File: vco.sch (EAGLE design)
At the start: 23 parts, among them IC2 CEM3340

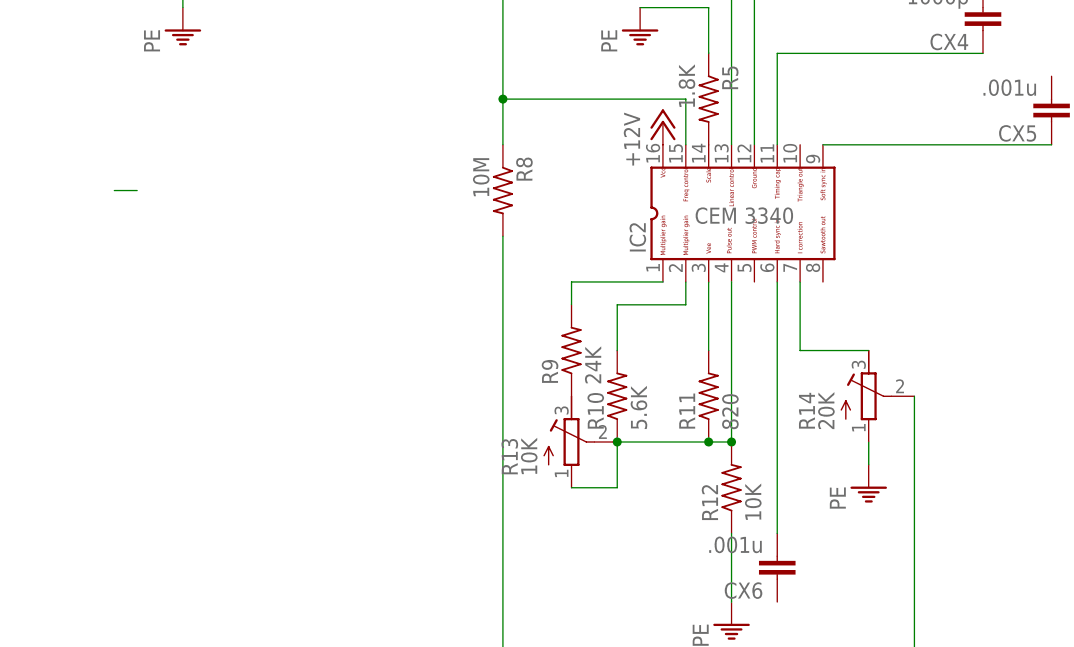
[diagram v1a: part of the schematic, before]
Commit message: Changed pots, added connector, updated org file.
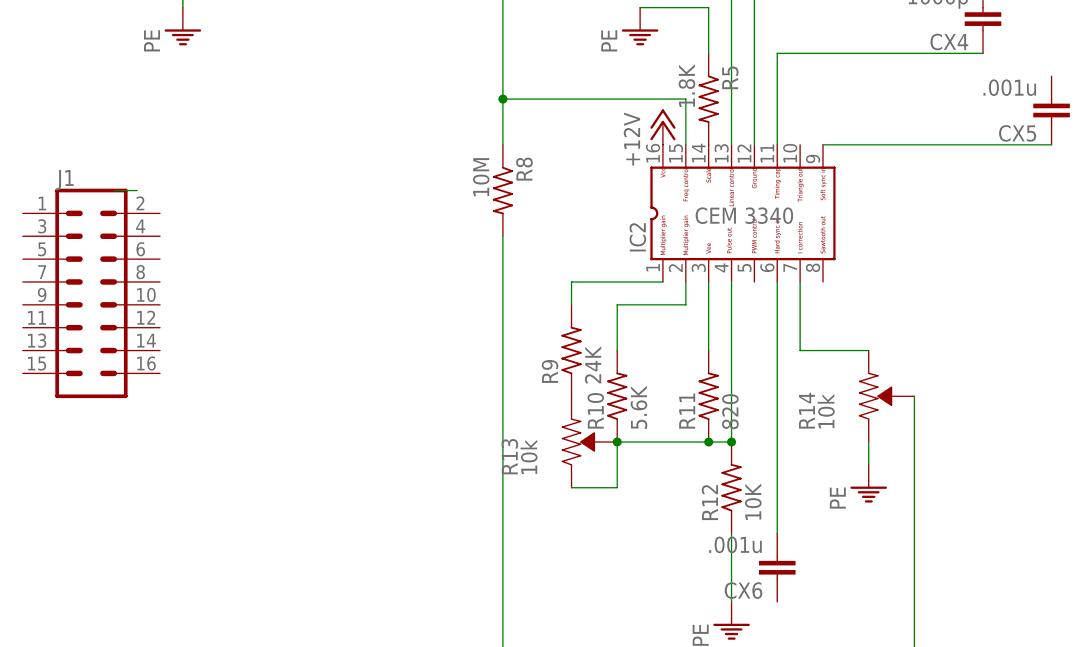
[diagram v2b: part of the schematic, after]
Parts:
- added J1: (no value), SparkFun-Connectors:CONN_08X2_SHROUD
- R13: value 10K -> 10k; device rcl:R-TRIMM4G/J -> SparkFun-Resistors:TRIMPOT-PTH-10MM-KNOB-1/2W-10%
- R14: value 20K -> 10k; device rcl:R-TRIMM4G/J -> SparkFun-Resistors:TRIMPOT-PTH-10MM-KNOB-1/2W-10%
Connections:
- net N$11: now also R13.CCW; no longer R13.E
- net N$13: now also R14.CCW; no longer R14.E
- net N$14: now also R13.CW, R13.WIPER; no longer R13.A, R13.S
- net N$17: now also R14.WIPER; no longer R14.S
- net PE: now also R14.CW; no longer R14.A

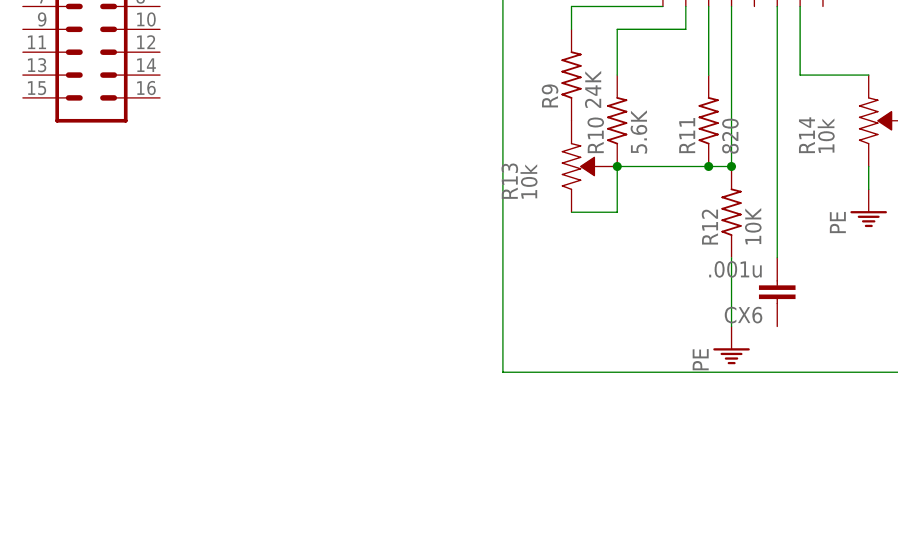
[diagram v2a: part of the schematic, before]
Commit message: Added -5v regulator as option. fixed pin 4.
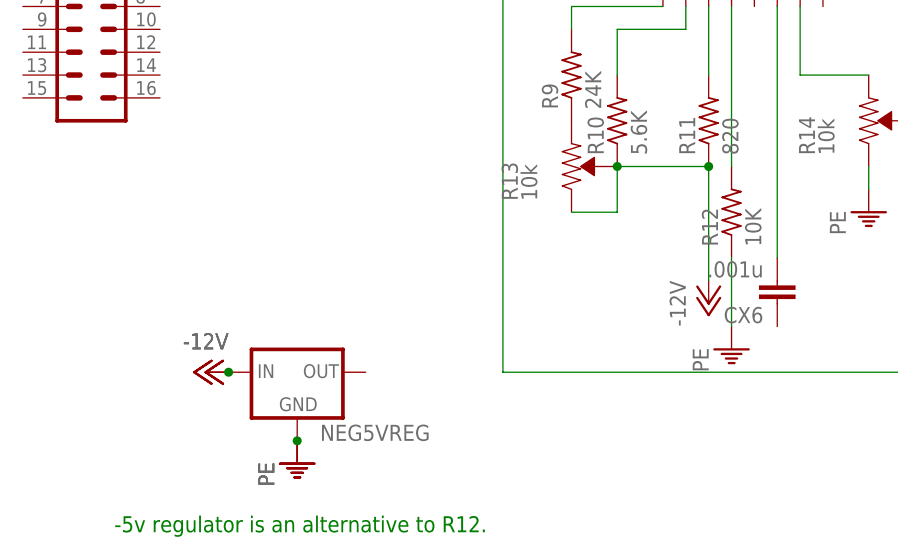
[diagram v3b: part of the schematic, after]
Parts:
- added NEG5VREG: (no value), SparkFun-IC-Power:V_REG_78XXTO-92_UNTESTED
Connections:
- removed net N$14: IC2.4, R10.1, R11.1, R12.2, R13.CW, R13.WIPER
- new net -12V: NEG5VREG.IN, R10.1, R11.1, R13.CW, R13.WIPER
- new net N$18: IC2.4, R12.2
- net PE: now also NEG5VREG.GND
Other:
- note added: "-5v regulator is an alternative to R12."

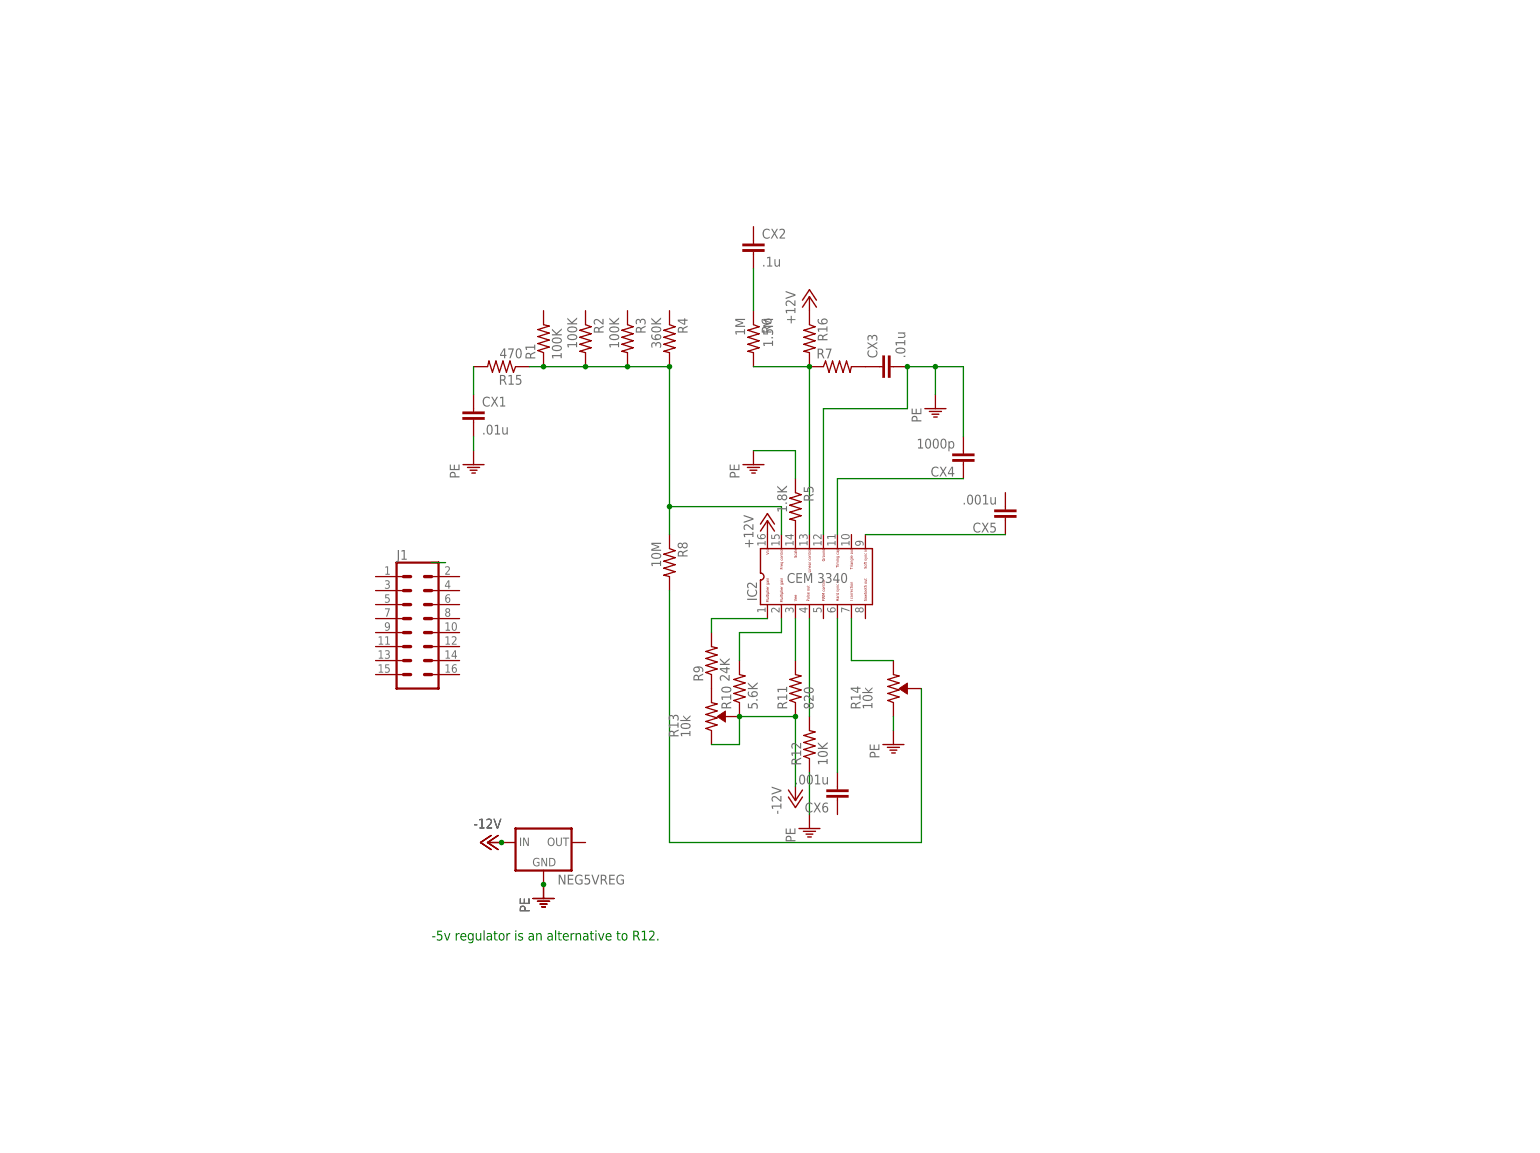
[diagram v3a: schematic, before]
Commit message: Updated todo list. Updated form factors of capacitors.
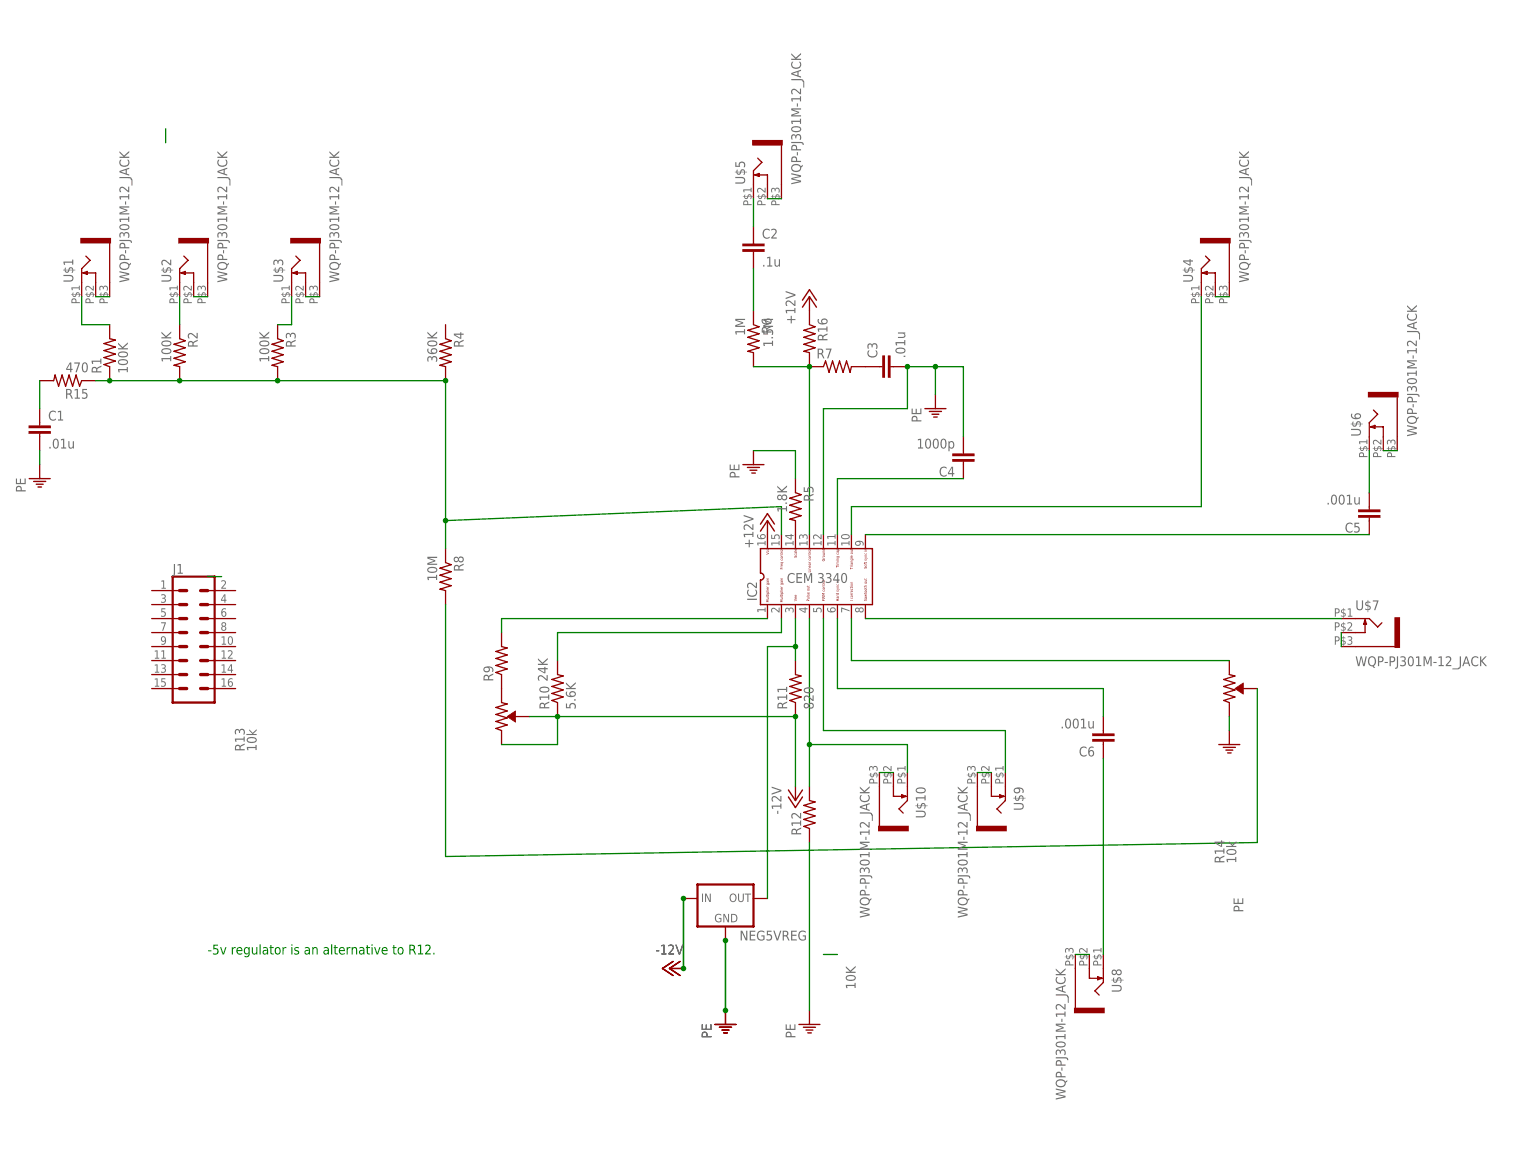
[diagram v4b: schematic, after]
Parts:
- removed CX1, CX3: .01u, rcl:CXXC10B5
- removed CX2: .1u, rcl:CXXC10B5
- removed CX4: 1000p, rcl:CXXC10B5
- removed CX5, CX6: .001u, rcl:CXXC10B5
- added C1, C3: .01u, rcl:C-EU050-025X075
- added C2: .1u, rcl:C-EU050-025X075
- added C4: 1000p, rcl:C-EU050-025X075
- added C5, C6: .001u, rcl:C-EU050-025X075
- added U$1, U$10, U$2, U$3, U$4, U$5, U$6, U$7, U$8, U$9: WQP-PJ301M-12_JACK, thonkiconn:WQP-PJ301M-12_JACK
- R1, R10, R11, R12, R15, R16, R2, R3, R4, R5, R6, R7, R8, R9: device rcl:R-US_0204/7 -> rcl:R-US_0207/10
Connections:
- new net N$14: R1.2, U$1.2
- new net N$19: U$1.1, U$1.3
- new net N$20: R2.1, U$2.2
- new net N$22: R3.1, U$3.2
- new net N$23: IC2.10, U$4.2
- new net N$24: C2.1, U$5.2
- new net N$25: U$2.1, U$2.3
- new net N$26: U$3.1, U$3.3
- new net N$27: U$5.1, U$5.3
- new net N$28: U$4.1, U$4.3
- new net N$29: C5.2, U$6.2
- new net N$30: U$6.1, U$6.3
- new net N$31: IC2.8, U$7.2
- new net N$32: U$7.1, U$7.3
- new net N$33: U$8.1, U$8.3
- new net N$34: C6.1, U$8.2
- new net N$35: IC2.5, U$9.2
- new net N$36: U$9.1, U$9.3
- new net N$39: U$10.1, U$10.3
- net N$12: now also NEG5VREG.OUT
- net N$15: now also C6.2; no longer CX6.2
- net N$18: now also U$10.2
- net N$2: now also C1.1; no longer CX1.1
- net N$5: now also C2.2; no longer CX2.2
- net N$6: now also C3.1; no longer CX3.1
- net N$7: now also C4.1; no longer CX4.1
- net N$9: now also C5.1; no longer CX5.1
- net PE: now also C1.2, C3.2, C4.2; no longer CX1.2, CX3.2, CX4.2
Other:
- moved on the sheet: J1, NEG5VREG, R1, R10, R12, R13, R14, R15, R2, R3, R4, R8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
